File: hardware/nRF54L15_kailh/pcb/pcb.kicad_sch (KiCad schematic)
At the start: 145 parts, among them M1 Ezurio BL54L15 (nrf54L15) mod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, SW1 SW_DIP_x01, SW2 SW_DIP_x01, Y1 32.768 kHz

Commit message: M  hardware/nRF54L15_gateron/pcb/pcb.kicad_prl M  hardware/nRF54L15_kailh/border.py M  hardware/nRF54L15_kailh/pcb/pcb.kicad_pcb M  hardware/nRF54L15_kailh/pcb/pcb.kicad_prl M  hardware/nRF54L15_kailh/pcb/pcb.kicad_sch M  hardware/nRF54L15_kailh/placefp.py A  hardware/nRF54L15_kailh/tmr-footprints/SMTSO_M2.kicad_mod M  hardware/nRF54L15_kailh/tmr-footprints/TMR2615-DFN-3L-1.6x1.6.kicad_mod M  hardware/nRF54L15_kailh/tracks.py
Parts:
- Hs1: renamed from H1; footprint MountingHole:MountingHole_2.2mm_M2_ISO7380_Pad_TopBottom -> tmr-lib:SMTSO_M2
- Hs10: renamed from Hs9; footprint MountingHole:MountingHole_2.2mm_M2_ISO7380_Pad_TopBottom -> tmr-lib:SMTSO_M2
- Hs2: renamed from Hs1; footprint MountingHole:MountingHole_2.2mm_M2_ISO7380_Pad_TopBottom -> tmr-lib:SMTSO_M2
- Hs3: renamed from Hs2; footprint MountingHole:MountingHole_2.2mm_M2_ISO7380_Pad_TopBottom -> tmr-lib:SMTSO_M2
- Hs4: renamed from Hs3; footprint MountingHole:MountingHole_2.2mm_M2_ISO7380_Pad_TopBottom -> tmr-lib:SMTSO_M2
- Hs5: renamed from Hs4; footprint MountingHole:MountingHole_2.2mm_M2_ISO7380_Pad_TopBottom -> tmr-lib:SMTSO_M2
- Hs6: renamed from Hs5; footprint MountingHole:MountingHole_2.2mm_M2_ISO7380_Pad_TopBottom -> tmr-lib:SMTSO_M1.6
- Hs7: renamed from Hs6; footprint MountingHole:MountingHole_2.2mm_M2_ISO7380_Pad_TopBottom -> tmr-lib:SMTSO_M1.6
- Hs8: renamed from Hs7; footprint MountingHole:MountingHole_2.2mm_M2_ISO7380_Pad_TopBottom -> tmr-lib:SMTSO_M1.6
- Hs9: renamed from Hs8; footprint MountingHole:MountingHole_2.2mm_M2_ISO7380_Pad_TopBottom -> tmr-lib:SMTSO_M1.6
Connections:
- net AIN2: now also MUXA1.9 (D3); no longer MUXA1.12 (D4)
- net AIN3: now also MUXA1.12 (D4); no longer MUXA1.9 (D3)
- net AIN4: now also MUXA2.9 (D3); no longer MUXA2.7 (D2)
- net AIN5: now also MUXA2.12 (D4); no longer MUXA2.9 (D3)
- net AIN7: now also MUXA2.7 (D2); no longer MUXA2.12 (D4)
- net ANA_65: now also MUXB8.9 (S8); no longer MUXB8.12 (S5)
- net ANA_66: now also MUXB8.12 (S5); no longer MUXB8.11 (S6)
- net ANA_67: now also MUXB8.11 (S6); no longer MUXB8.10 (S7)
- net ANA_68: now also MUXB8.10 (S7); no longer MUXB8.9 (S8)

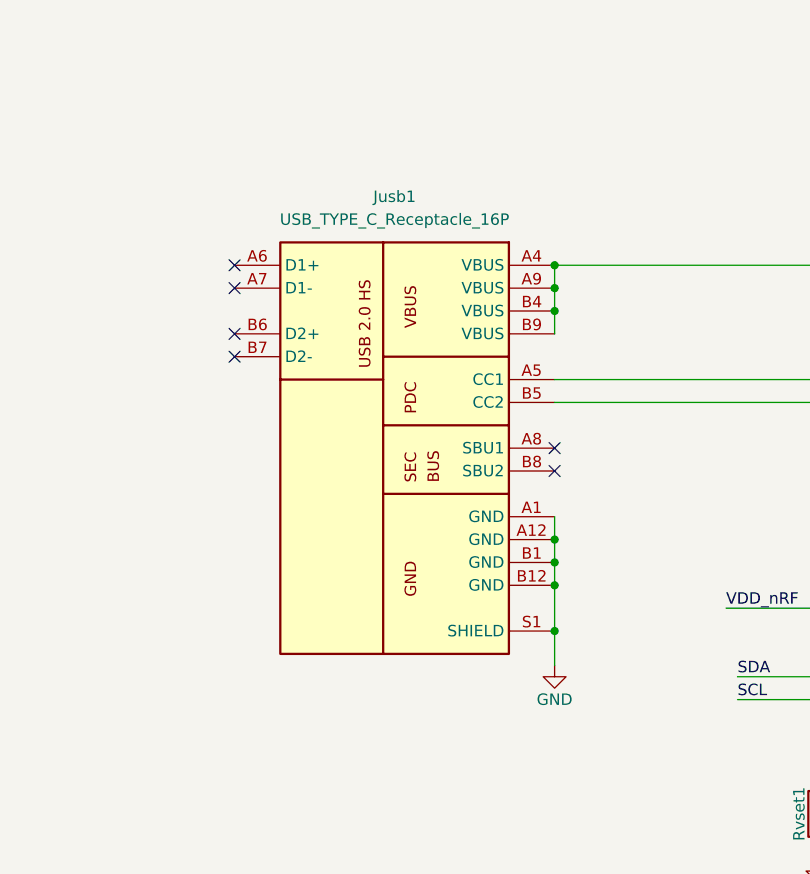
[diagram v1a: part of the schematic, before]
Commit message: M  hardware/nRF54L15_kailh/border.py A  hardware/nRF54L15_kailh/pcb/pcb-F_Fab.dxf M  hardware/nRF54L15_kailh/pcb/pcb.kicad_pcb M  hardware/nRF54L15_kailh/pcb/pcb.kicad_prl M  hardware/nRF54L15_kailh/pcb/pcb.kicad_sch M  hardware/nRF54L15_kailh/placefp.py A  hardware/nRF54L15_kailh/plate/plate-User_5.dxf M  hardware/nRF54L15_kailh/plate/plate.kicad_pcb M  hardware/nRF54L15_kailh/plate/plate.kicad_sch A  hardware/nRF54L15_kailh/tmr-footprints/MountingHole_1.7mm_M1.6_NoPad.kicad_mod M  hardware/nRF54L15_kailh/tmr-footprints/MountingHole_2.1mm_M2_NoPad.kicad_mod M  hardware/nRF54L15_kailh/tmr-footprints/Stabilizer_Lowpro_2U.kicad_mod R  hardware/nRF54L15_kailh/tmr-footprints/Switch_Cutout_1.25u.kicad_mod -> hardware/nRF54L15_kailh/tmr-footprints/Switch_Cutout_1.25u_powdercoat.kicad_mod R  hardware/nRF54L15_kailh/tmr-footprints/Switch_Cutout_1.75u.kicad_mod -> hardware/nRF54L15_kailh/tmr-footprints/Switch_Cutout_1.75u_powdercoat.kicad_mod R  hardware/nRF54L15_kailh/tmr-footprints/Switch_Cutout_2u.kicad_mod -> hardware/nRF54L15_kailh/tmr-footprints/Switch_Cutout_2u_powdercoat.kicad_mod R  hardware/nRF54L15_kailh/tmr-footprints/Switch_Cutout.kicad_mod -> hardware/nRF54L15_kailh/tmr-footprints/Switch_Cutout_powdercoat.kicad_mod A  hardware/nRF54L15_kailh/tmr-footprints/USB_C_Receptacle_GCT_USB4125-xx-x_6P_TopMnt_Horizontal.kicad_mod
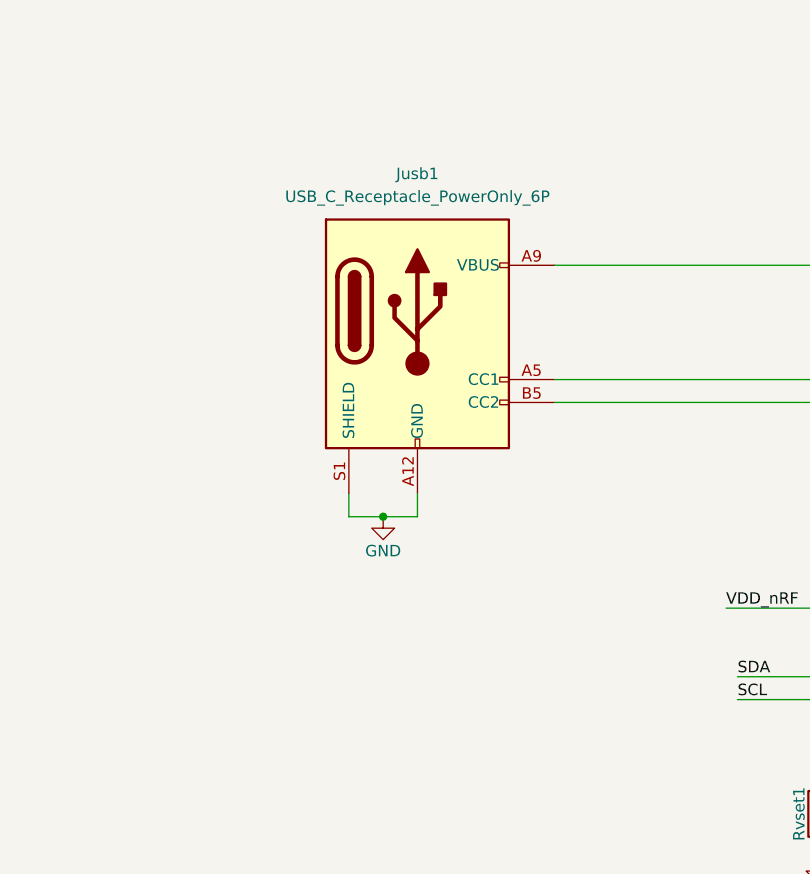
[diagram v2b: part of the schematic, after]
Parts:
- removed Jusb1: USB_TYPE_C_Receptacle_16P, tmr-lib:USB_C_Receptacle_GCT_USB4085, symbol tmr-lib:USB_TYPE_C_Receptacle_16P
- added Jusb1: USB_C_Receptacle_PowerOnly_6P, tmr-lib:USB_C_Receptacle_GCT_USB4125-xx-x_6P_TopMnt_Horizontal, symbol Connector:USB_C_Receptacle_PowerOnly_6P
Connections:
- net GND: now also Jusb1.A12 (GND), Jusb1.B12 (GND), Jusb1.S1 (SHIELD)
- net at C16.1, PMIC1.21 (VBUS): now also Jusb1.A9 (VBUS), Jusb1.B9 (VBUS)
- net at PMIC1.23 (CC1): now also Jusb1.A5 (CC1)
- net at PMIC1.24 (CC2): now also Jusb1.B5 (CC2)
- no-connect marks 24 -> 18

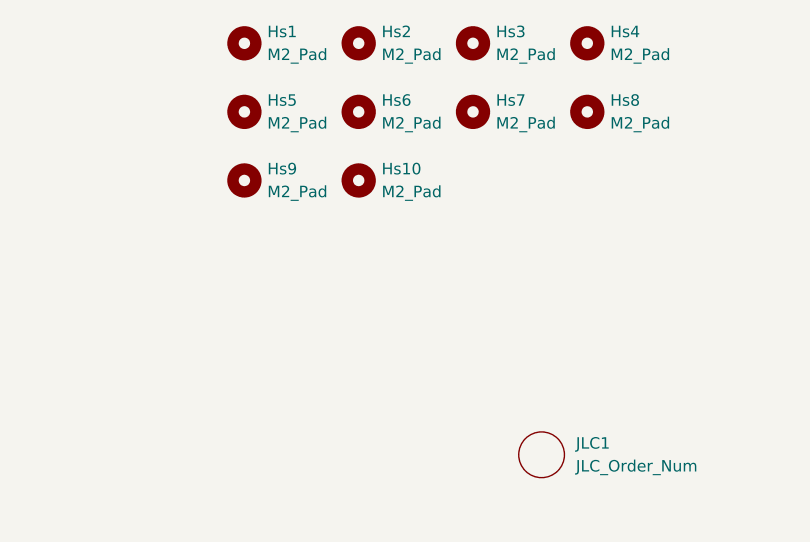
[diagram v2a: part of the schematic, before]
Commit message: M  hardware/nRF54L15_kailh/border.py M  hardware/nRF54L15_kailh/botcover/botcover.kicad_pcb M  hardware/nRF54L15_kailh/botcover/botcover.kicad_sch M  hardware/nRF54L15_kailh/pcb/pcb.kicad_pcb M  hardware/nRF54L15_kailh/pcb/pcb.kicad_sch M  hardware/nRF54L15_kailh/placefp.py A  hardware/nRF54L15_kailh/tmr-footprints/MountingHole_1.5mm_M1.4_NoPad.kicad_mod R  hardware/nRF54L15_kailh/tmr-footprints/SMTSO_M1.6.kicad_mod -> hardware/nRF54L15_kailh/tmr-footprints/SMTSO_M1.4_M1.6.kicad_mod
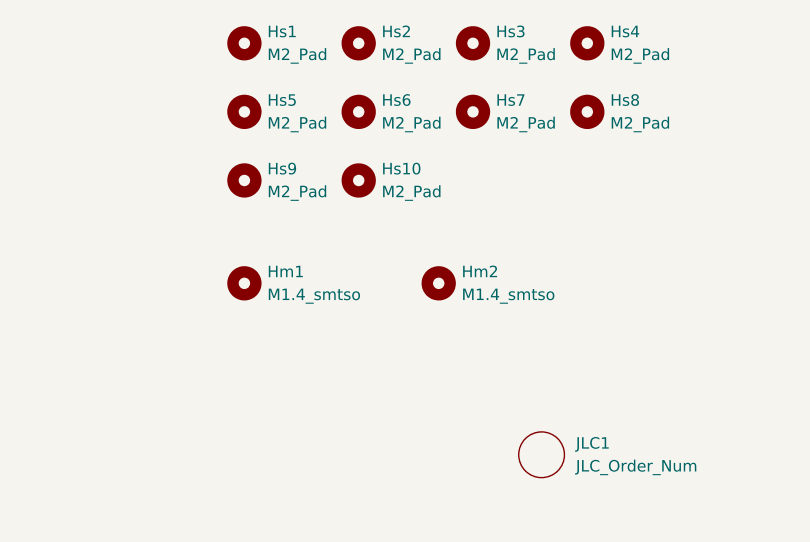
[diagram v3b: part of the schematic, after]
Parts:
- added Hm1, Hm2: M1.4_smtso, tmr-lib:SMTSO_M1.4_M1.6, symbol Mechanical:MountingHole
- Hs6, Hs7, Hs8, Hs9: footprint tmr-lib:SMTSO_M1.6 -> tmr-lib:SMTSO_M1.4_M1.6
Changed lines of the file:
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@@
 	)
 	(symbol
+		(lib_id "Mechanical:MountingHole")
+		(at 359.41 391.16 0)
+		(unit 1)
+		(exclude_from_sim no)
+		(in_bom no)
+		(on_board yes)
+		(dnp no)
+		(fields_autoplaced yes)
+		(property "Reference" "Hm1"
+			(at 361.95 389.8899 0)
+			(effects
+				(font
+					(size 1.27 1.27)
+				)
+				(justify left)
+			)
+		)
+		(property "Value" "M1.4_smtso"
+			(at 361.95 392.4299 0)
+			(effects
+				(font
+					(size 1.27 1.27)
+				)
+				(justify left)
+			)
+		)
+		(property "Footprint" "tmr-lib:SMTSO_M1.4_M1.6"
+			(at 359.41 391.16 0)
+			(effects
+				(font
+					(size 1.27 1.27)
+				)
+				(hide yes)
+			)
+		)
+		(property "Datasheet" "~"
+			(at 359.41 391.16 0)
+			(effects
+				(font
+					(size 1.27 1.27)
+				)
+				(hide yes)
+			)
+		)
+		(property "Description" "Mounting Hole without connection"
+			(at 359.41 391.16 0)
+			(effects
+				(font
+					(size 1.27 1.27)
+				)
+				(hide yes)
+			)
+		)
+		(instances
+			(project "pcb"
+				(path "/672ae9a0-2ac9-4023-9977-e9626ff99f32"
+					(reference "Hm1")
+					(unit 1)
+				)
+			)
+		)
+	)
+	(symbol
 		(lib_id "Device:LED_Small_Filled")
 		(at 116.84 349.25 180)
@@
 			)
 		)
-		(property "Footprint" "tmr-lib:SMTSO_M1.6"
+		(property "Footprint" "tmr-lib:SMTSO_M1.4_M1.6"
 			(at 397.51 372.11 0)
 			(effects
@@
 			)
 		)
-		(property "Footprint" "tmr-lib:SMTSO_M1.6"
+		(property "Footprint" "tmr-lib:SMTSO_M1.4_M1.6"
 			(at 372.11 372.11 0)
 			(effects
@@
 			)
 		)
-		(property "Footprint" "tmr-lib:SMTSO_M1.6"
+		(property "Footprint" "tmr-lib:SMTSO_M1.4_M1.6"
 			(at 359.41 379.73 0)
 			(effects
@@
 			)
 		)
-		(property "Footprint" "tmr-lib:SMTSO_M1.6"
+		(property "Footprint" "tmr-lib:SMTSO_M1.4_M1.6"
 			(at 384.81 372.11 0)
 			(effects
@@
 					(unit 1)
 				)
+			)
+		)
+	)
+	(symbol
+		(lib_id "Mechanical:MountingHole")
+		(at 381 391.16 0)
+		(unit 1)
+		(exclude_from_sim no)
+		(in_bom no)
+		(on_board yes)
+		(dnp no)
+		(fields_autoplaced yes)
+		(property "Reference" "Hm2"
+			(at 383.54 389.8899 0)
+			(effects
+				(font
+					(size 1.27 1.27)
+				)
+				(justify left)
+			)
+		)
+		(property "Value" "M1.4_smtso"
+			(at 383.54 392.4299 0)
+			(effects
+				(font
+					(size 1.27 1.27)
+				)
+				(justify left)
+			)
+		)
+		(property "Footprint" "tmr-lib:SMTSO_M1.4_M1.6"
+			(at 381 391.16 0)
+			(effects
+				(font
+					(size 1.27 1.27)
+				)
+				(hide yes)
+			)
+		)
+		(property "Datasheet" "~"
+			(at 381 391.16 0)
+			(effects
+				(font
+					(size 1.27 1.27)
+				)
+				(hide yes)
+			)
+		)
+		(property "Description" "Mounting Hole without connection"
+			(at 381 391.16 0)
+			(effects
+				(font
+					(size 1.27 1.27)
+				)
+				(hide yes)
+			)
+		)
+		(instances
+			(project "pcb"
+				(path "/672ae9a0-2ac9-4023-9977-e9626ff99f32"
+					(reference "Hm2")
+					(unit 1)
+				)
